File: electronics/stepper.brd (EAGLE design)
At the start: 50.8 x 44.5 mm, 17 parts, among them J1 1-770969-0, J2 1-770968-0, J3 DF1BZ-8DP-2.5DSA, J4 S4B-XH-A, U1 ATMEGA328PB32-TQFP

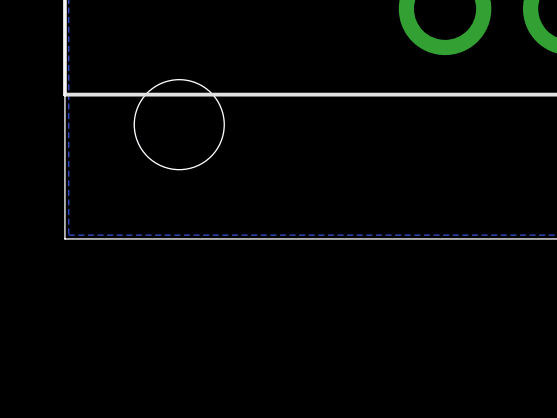
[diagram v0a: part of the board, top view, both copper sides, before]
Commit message: Added pull-up on RESET
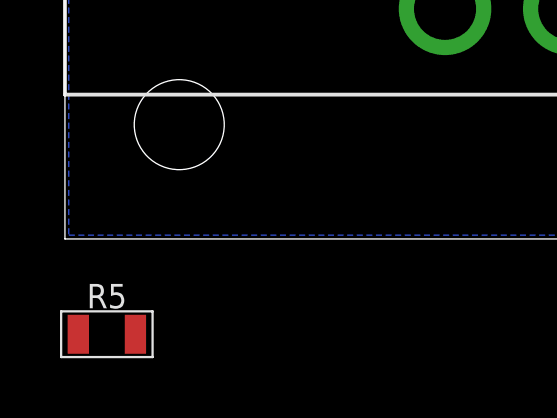
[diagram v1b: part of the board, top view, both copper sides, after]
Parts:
- added R5: 10k, Zach:0805
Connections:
- net +3V3: now also R5.P$2
- net RESET: now also R5.P$1
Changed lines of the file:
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@@
 <attribute name="NAME" x="35.941" y="23.6864" size="0.8128" layer="25" rot="R180" align="bottom-center"/>
+</element>
+<element name="R5" library="Zach" package="0805" value="10k" x="1.397" y="-3.175" smashed="yes">
+<attribute name="NAME" x="1.397" y="-2.3114" size="0.8128" layer="25" align="bottom-center"/>
 </element>
 </elements>
@@
 <wire x1="41.51" y1="29.102" x2="41.402" y2="28.994" width="0.4064" layer="1"/>
 <wire x1="41.402" y1="28.994" x2="41.402" y2="26.035" width="0.4064" layer="1"/>
+<contactref element="R5" pad="P$2"/>
+<wire x1="2.3495" y1="-3.175" x2="16.81" y2="7.671" width="0" layer="19" extent="1-1"/>
 </signal>
 <signal name="SDL">
@@
 <wire x1="35.052" y1="42.291" x2="27.432" y2="42.291" width="0.4064" layer="1"/>
 <wire x1="26.797" y1="21.717" x2="29.8054" y2="18.7086" width="0.4064" layer="1"/>
+<contactref element="R5" pad="P$1"/>
+<wire x1="0.4445" y1="-3.175" x2="38.12" y2="8.91" width="0" layer="19" extent="1-1"/>
 </signal>
 <signal name="RX">

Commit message: finished stepper
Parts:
- R5: device Zach:0805 -> Zach:0402
- moved R5 34.4 mm to (33.9, 8.00), turned to 270 degrees
- moved C4 0.90 mm to (36.6, 29.1), turned to 0 degrees
- flipped A1 to the bottom, turned to 270 degrees
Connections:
- net +3V3: now also R5.2; no longer R5.P$2
- net DIRECTION: now also U1.32; no longer U1.11
- net MODE_1: now also U1.10; no longer U1.1
- net MODE_2: now also U1.9; no longer U1.2
- net MODE_3: now also U1.6; no longer U1.9
- net MOTOR_1A: now also A1.3; no longer A1.4
- net MOTOR_1B: now also A1.4; no longer A1.3
- net RESET: now also R5.1; no longer R5.P$1
- net RST: now also U1.3; no longer U1.14
- net SLEEP: now also U1.2; no longer U1.13
- net STEP: now also U1.1; no longer U1.10
- net ~EN: now also U1.11; no longer U1.32
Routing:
- net +12V: track 24.8 -> 6.03 mm
- net +3V3: track 85.7 -> 100.1 mm
- net RST: track 18.2 -> 9.78 mm, vias 1 -> 0
- net MODE_3: track 17.7 -> 9.72 mm, vias 2 -> 0
- net SLEEP: track 15.3 -> 10.5 mm, vias 1 -> 0
- net MODE_2: track 10.5 -> 13.3 mm
- net MODE_1: track 11.2 -> 13.4 mm
- net STEP: track 13.1 -> 11.2 mm
- net MOTOR_1A: track 8.94 -> 7.89 mm
- net MOTOR_1B: track 5.78 -> 6.66 mm
- net DIRECTION: track 13.9 -> 13.1 mm
- net N$4: track 0.00 -> 0.76 mm, vias 0 -> 1
- net ~EN: track 13.1 -> 13.8 mm
- net MOTOR_2A: track 6.09 -> 6.31 mm, vias 0 -> 1
- net GND: track 2.17 -> 2.14 mm, vias 8 -> 7
